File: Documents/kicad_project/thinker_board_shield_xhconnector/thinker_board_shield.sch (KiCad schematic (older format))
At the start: 8 parts, among them J2 Thinker_board_S, U1 XH_S, U2 1PIN, U3 XH_4PIN

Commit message: add big wire /before auto-router
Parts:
- added U4: 2_pin, hoshina_library:2_pin, symbol hoshina_library:2_pin
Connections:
- net +3V3: now also U4.1
- net GND: now also U4.2
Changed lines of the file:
@@
 Wire Wire Line
 	4800 2950 4800 3200
+$Comp
+L hoshina_library:2_pin U4
+U 1 1 5D790A94
+P 2650 4450
+F 0 "U4" H 2778 4501 50  0000 L CNN
+F 1 "2_pin" H 2778 4410 50  0000 L CNN
+F 2 "hoshina_library:2_pin" H 2650 4300 50  0001 C CNN
+F 3 "" H 2650 4300 50  0001 C CNN
+	1    2650 4450
+	1    0    0    -1
+$EndComp
+Text GLabel 2550 4500 0    50   Input ~ 0
+GND
+$Comp
+L power:+3.3V #PWR0103
+U 1 1 5D7912AC
+P 2550 4400
+F 0 "#PWR0103" H 2550 4250 50  0001 C CNN
+F 1 "+3.3V" V 2565 4528 50  0000 L CNN
+F 2 "" H 2550 4400 50  0001 C CNN
+F 3 "" H 2550 4400 50  0001 C CNN
+	1    2550 4400
+	0    -1   -1   0
+$EndComp
 $EndSCHEMATC

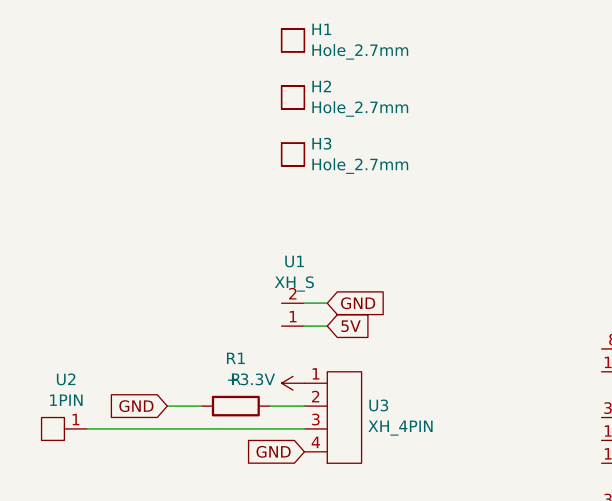
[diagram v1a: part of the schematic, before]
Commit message: add parts and set position
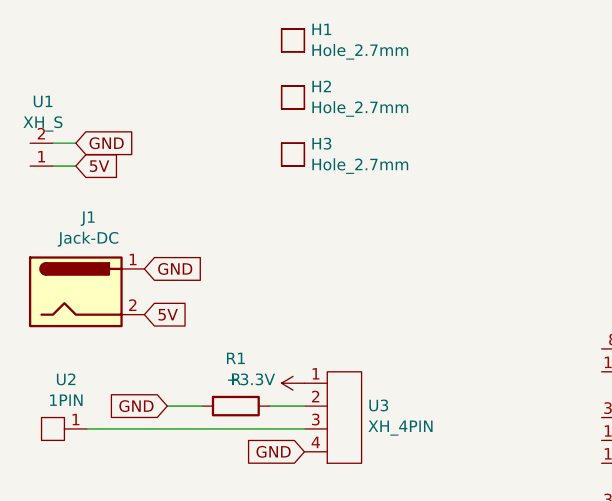
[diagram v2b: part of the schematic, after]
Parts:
- added J1: Jack-DC, hoshina_library:DCJ, symbol Connector:Jack-DC
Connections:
- net 5V: now also J1.2
- net GND: now also J1.1
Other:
- moved on the sheet: U1
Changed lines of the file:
@@
 	1    0    0    -1
 $EndComp
-Text GLabel 2700 3500 2    50   Input ~ 0
+Text GLabel 1900 3450 2    50   Input ~ 0
 5V
-Text GLabel 2700 3400 2    50   Input ~ 0
+Text GLabel 1900 3250 2    50   Input ~ 0
 GND
 Text GLabel 4450 3000 0    50   Input ~ 0
@@
 Connection ~ 4900 5900
 Wire Wire Line
-	2600 3400 2700 3400
-Wire Wire Line
-	2700 3500 2600 3500
+	1500 2700 1600 2700
+Wire Wire Line
+	1600 2800 1500 2800
 $Comp
 L hoshina_library:XH_S U1
 U 1 1 5D710EE3
-P 2600 3400
-F 0 "U1" H 2643 3219 50  0000 C CNN
-F 1 "XH_S" H 2643 3310 50  0000 C CNN
-F 2 "hoshina_library:S2B-XH-A" H 2600 3300 50  0001 C CNN
-F 3 "" H 2600 3300 50  0001 C CNN
-	1    2600 3400
+P 1500 2700
+F 0 "U1" H 1543 2519 50  0000 C CNN
+F 1 "XH_S" H 1543 2610 50  0000 C CNN
+F 2 "hoshina_library:S2B-XH-A" H 1500 2600 50  0001 C CNN
+F 3 "" H 1500 2600 50  0001 C CNN
+	1    1500 2700
 	-1   0    0    1
 $EndComp
@@
 	0    -1   -1   0
 $EndComp
+$Comp
+L Connector:Jack-DC J1
+U 1 1 5D792B55
+P 1600 3350
+F 0 "J1" H 1657 3675 50  0000 C CNN
+F 1 "Jack-DC" H 1657 3584 50  0000 C CNN
+F 2 "hoshina_library:DCJ" H 1650 3310 50  0001 C CNN
+F 3 "~" H 1650 3310 50  0001 C CNN
+	1    1600 3350
+	1    0    0    -1
+$EndComp
+Text GLabel 1600 2800 2    50   Input ~ 0
+5V
+Text GLabel 1600 2700 2    50   Input ~ 0
+GND
 $EndSCHEMATC

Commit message: change to raspi
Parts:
- added s1, s2, s3, s4: connectable_smd, hoshina_library:connectable_smd, symbol hoshina_library:connectable_smd
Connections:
- net +3V3: now also s3.2; no longer U3.1
- net Raspi_GPIO26: now reaches J2.37 (GPIO26)
- net Raspi_GPIO26: now also s2.2
- net Raspi_SCL: now reaches J2.40 (GPIO21/SCLK1)
- net Raspi_SCL: now also s1.2
- net Raspi_TX: now reaches J2.8 (GPIO14/TXD)
- net Raspi_TX: now also s4.2
- net at U2.1, U3.3: now also s1.1, s2.1
- new net: U3.1, s3.1, s4.1
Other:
- moved on the sheet: J1, R1, U1, U2, U3, U4
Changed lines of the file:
@@
 	1    0    0    -1
 $EndComp
-Text GLabel 1900 3450 2    50   Input ~ 0
+Text GLabel 1800 2800 2    50   Input ~ 0
 5V
-Text GLabel 1900 3250 2    50   Input ~ 0
+Text GLabel 1800 2600 2    50   Input ~ 0
 GND
 Text GLabel 4450 3000 0    50   Input ~ 0
@@
 Connection ~ 4900 5900
 Wire Wire Line
-	1500 2700 1600 2700
-Wire Wire Line
-	1600 2800 1500 2800
+	1400 2050 1500 2050
+Wire Wire Line
+	1500 2150 1400 2150
 $Comp
 L hoshina_library:XH_S U1
 U 1 1 5D710EE3
-P 1500 2700
-F 0 "U1" H 1543 2519 50  0000 C CNN
-F 1 "XH_S" H 1543 2610 50  0000 C CNN
-F 2 "hoshina_library:S2B-XH-A" H 1500 2600 50  0001 C CNN
-F 3 "" H 1500 2600 50  0001 C CNN
-	1    1500 2700
+P 1400 2050
+F 0 "U1" H 1443 1869 50  0000 C CNN
+F 1 "XH_S" H 1443 1960 50  0000 C CNN
+F 2 "hoshina_library:S2B-XH-A" H 1400 1950 50  0001 C CNN
+F 3 "" H 1400 1950 50  0001 C CNN
+	1    1400 2050
 	-1   0    0    1
 $EndComp
@@
 L hoshina_library:XH_4PIN U3
 U 1 1 5D76ADEE
-P 2600 3950
-F 0 "U3" H 2878 4051 50  0000 L CNN
-F 1 "XH_4PIN" H 2878 3960 50  0000 L CNN
-F 2 "hoshina_library:XH4PIN_S" H 2600 3750 50  0001 C CNN
-F 3 "" H 2600 3750 50  0001 C CNN
-	1    2600 3950
+P 2550 4550
+F 0 "U3" H 2828 4651 50  0000 L CNN
+F 1 "XH_4PIN" H 2828 4560 50  0000 L CNN
+F 2 "hoshina_library:XH4PIN_S" H 2550 4350 50  0001 C CNN
+F 3 "" H 2550 4350 50  0001 C CNN
+	1    2550 4550
 	1    0    0    -1
 $EndComp
@@
 L power:+3.3V #PWR0101
 U 1 1 5D76B7AA
-P 2600 3750
-F 0 "#PWR0101" H 2600 3600 50  0001 C CNN
-F 1 "+3.3V" V 2615 3878 50  0000 L CNN
-F 2 "" H 2600 3750 50  0001 C CNN
-F 3 "" H 2600 3750 50  0001 C CNN
-	1    2600 3750
+P 1800 3450
+F 0 "#PWR0101" H 1800 3300 50  0001 C CNN
+F 1 "+3.3V" V 1815 3578 50  0000 L CNN
+F 2 "" H 1800 3450 50  0001 C CNN
+F 3 "" H 1800 3450 50  0001 C CNN
+	1    1800 3450
 	0    -1   -1   0
 $EndComp
-Text GLabel 2000 3850 0    50   Input ~ 0
+Text GLabel 1950 4450 0    50   Input ~ 0
 GND
 $Comp
 L Device:R R1
 U 1 1 5D76C583
-P 2300 3850
-F 0 "R1" V 2093 3850 50  0000 C CNN
-F 1 "R" V 2184 3850 50  0000 C CNN
-F 2 "hoshina_library:register_0603" V 2230 3850 50  0001 C CNN
-F 3 "~" H 2300 3850 50  0001 C CNN
-	1    2300 3850
+P 2250 4450
+F 0 "R1" V 2043 4450 50  0000 C CNN
+F 1 "R" V 2134 4450 50  0000 C CNN
+F 2 "hoshina_library:register_0603" V 2180 4450 50  0001 C CNN
+F 3 "~" H 2250 4450 50  0001 C CNN
+	1    2250 4450
 	0    1    1    0
 $EndComp
 Wire Wire Line
-	2450 3850 2600 3850
-Wire Wire Line
-	2000 3850 2150 3850
-Text GLabel 2600 4050 0    50   Input ~ 0
+	2400 4450 2550 4450
+Wire Wire Line
+	1950 4450 2100 4450
+Text GLabel 2550 4650 0    50   Input ~ 0
 GND
 $Comp
 L hoshina_library:1PIN U2
 U 1 1 5D76DD85
-P 1650 3900
-F 0 "U2" H 1742 3735 50  0000 C CNN
-F 1 "1PIN" H 1742 3826 50  0000 C CNN
-F 2 "hoshina_library:1PIN" H 1750 3850 50  0001 C CNN
-F 3 "" H 1750 3850 50  0001 C CNN
-	1    1650 3900
-	-1   0    0    1
-$EndComp
-Wire Wire Line
-	2600 3950 1650 3950
+P 1600 4500
+F 0 "U2" H 1692 4335 50  0000 C CNN
+F 1 "1PIN" H 1692 4426 50  0000 C CNN
+F 2 "hoshina_library:1PIN" H 1700 4450 50  0001 C CNN
+F 3 "" H 1700 4450 50  0001 C CNN
+	1    1600 4500
+	-1   0    0    1
+$EndComp
+Wire Wire Line
+	2550 4550 1650 4550
 $Comp
 L power:+3.3V #PWR0102
@@
 L hoshina_library:2_pin U4
 U 1 1 5D790A94
-P 2650 4450
-F 0 "U4" H 2778 4501 50  0000 L CNN
-F 1 "2_pin" H 2778 4410 50  0000 L CNN
-F 2 "hoshina_library:2_pin" H 2650 4300 50  0001 C CNN
-F 3 "" H 2650 4300 50  0001 C CNN
-	1    2650 4450
-	1    0    0    -1
-$EndComp
-Text GLabel 2550 4500 0    50   Input ~ 0
+P 2650 5200
+F 0 "U4" H 2778 5251 50  0000 L CNN
+F 1 "2_pin" H 2778 5160 50  0000 L CNN
+F 2 "hoshina_library:2_pin" H 2650 5050 50  0001 C CNN
+F 3 "" H 2650 5050 50  0001 C CNN
+	1    2650 5200
+	1    0    0    -1
+$EndComp
+Text GLabel 2550 5250 0    50   Input ~ 0
 GND
 $Comp
 L power:+3.3V #PWR0103
 U 1 1 5D7912AC
-P 2550 4400
-F 0 "#PWR0103" H 2550 4250 50  0001 C CNN
-F 1 "+3.3V" V 2565 4528 50  0000 L CNN
-F 2 "" H 2550 4400 50  0001 C CNN
-F 3 "" H 2550 4400 50  0001 C CNN
-	1    2550 4400
+P 2550 5150
+F 0 "#PWR0103" H 2550 5000 50  0001 C CNN
+F 1 "+3.3V" V 2565 5278 50  0000 L CNN
+F 2 "" H 2550 5150 50  0001 C CNN
+F 3 "" H 2550 5150 50  0001 C CNN
+	1    2550 5150
 	0    -1   -1   0
 $EndComp
@@
 L Connector:Jack-DC J1
 U 1 1 5D792B55
-P 1600 3350
-F 0 "J1" H 1657 3675 50  0000 C CNN
-F 1 "Jack-DC" H 1657 3584 50  0000 C CNN
-F 2 "hoshina_library:DCJ" H 1650 3310 50  0001 C CNN
-F 3 "~" H 1650 3310 50  0001 C CNN
-	1    1600 3350
-	1    0    0    -1
-$EndComp
-Text GLabel 1600 2800 2    50   Input ~ 0
+P 1500 2700
+F 0 "J1" H 1557 3025 50  0000 C CNN
+F 1 "Jack-DC" H 1557 2934 50  0000 C CNN
+F 2 "hoshina_library:DCJ" H 1550 2660 50  0001 C CNN
+F 3 "~" H 1550 2660 50  0001 C CNN
+	1    1500 2700
+	1    0    0    -1
+$EndComp
+Text GLabel 1500 2150 2    50   Input ~ 0
 5V
-Text GLabel 1600 2700 2    50   Input ~ 0
-GND
+Text GLabel 1500 2050 2    50   Input ~ 0
+GND
+$Comp
+L hoshina_library:connectable_smd s3
+U 1 1 5D7B42C4
+P 1950 3450
+F 0 "s3" H 1950 3675 50  0000 C CNN
+F 1 "connectable_smd" H 1950 3584 50  0000 C CNN
+F 2 "hoshina_library:connectable_smd" H 1950 3300 50  0001 C CNN
+F 3 "" H 1950 3300 50  0001 C CNN
+	1    1950 3450
+	-1   0    0    1
+$EndComp
+$Comp
+L hoshina_library:connectable_smd s4
+U 1 1 5D7B9C1C
+P 1950 3800
+F 0 "s4" H 1950 4025 50  0000 C CNN
+F 1 "connectable_smd" H 1950 3934 50  0000 C CNN
+F 2 "hoshina_library:connectable_smd" H 1950 3650 50  0001 C CNN
+F 3 "" H 1950 3650 50  0001 C CNN
+	1    1950 3800
+	-1   0    0    1
+$EndComp
+Wire Wire Line
+	2100 3450 2550 3450
+Wire Wire Line
+	2550 3450 2550 3800
+Wire Wire Line
+	2100 3800 2550 3800
+Connection ~ 2550 3800
+Wire Wire Line
+	2550 3800 2550 4350
+Text GLabel 1800 3800 0    50   Input ~ 0
+Raspi_TX
+Text GLabel 3900 3600 0    50   Input ~ 0
+Raspi_TX
+$Comp
+L hoshina_library:connectable_smd s1
+U 1 1 5D7BBDD2
+P 1450 4800
+F 0 "s1" H 1450 5025 50  0000 C CNN
+F 1 "connectable_smd" H 1450 4934 50  0000 C CNN
+F 2 "hoshina_library:connectable_smd" H 1450 4650 50  0001 C CNN
+F 3 "" H 1450 4650 50  0001 C CNN
+	1    1450 4800
+	-1   0    0    1
+$EndComp
+Text GLabel 1300 4800 0    50   Input ~ 0
+Raspi_SCL
+$Comp
+L hoshina_library:connectable_smd s2
+U 1 1 5D7BCB7C
+P 1450 5200
+F 0 "s2" H 1450 5425 50  0000 C CNN
+F 1 "connectable_smd" H 1450 5334 50  0000 C CNN
+F 2 "hoshina_library:connectable_smd" H 1450 5050 50  0001 C CNN
+F 3 "" H 1450 5050 50  0001 C CNN
+	1    1450 5200
+	-1   0    0    1
+$EndComp
+Text GLabel 1300 5200 0    50   Input ~ 0
+Raspi_GPIO26
+Wire Wire Line
+	1600 4800 1650 4800
+Wire Wire Line
+	1650 4800 1650 4550
+Connection ~ 1650 4550
+Wire Wire Line
+	1650 4550 1600 4550
+Wire Wire Line
+	1650 4800 1650 5200
+Wire Wire Line
+	1650 5200 1600 5200
+Connection ~ 1650 4800
+Text GLabel 3900 4500 0    50   Input ~ 0
+Raspi_SCL
+Text GLabel 3900 5100 0    50   Input ~ 0
+Raspi_GPIO26
 $EndSCHEMATC
